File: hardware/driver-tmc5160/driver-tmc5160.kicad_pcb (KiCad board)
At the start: 2 copper layers, 30 x 30 mm, 34 parts, among them J1 Micro-Fit, U1 TMC5160A-TA

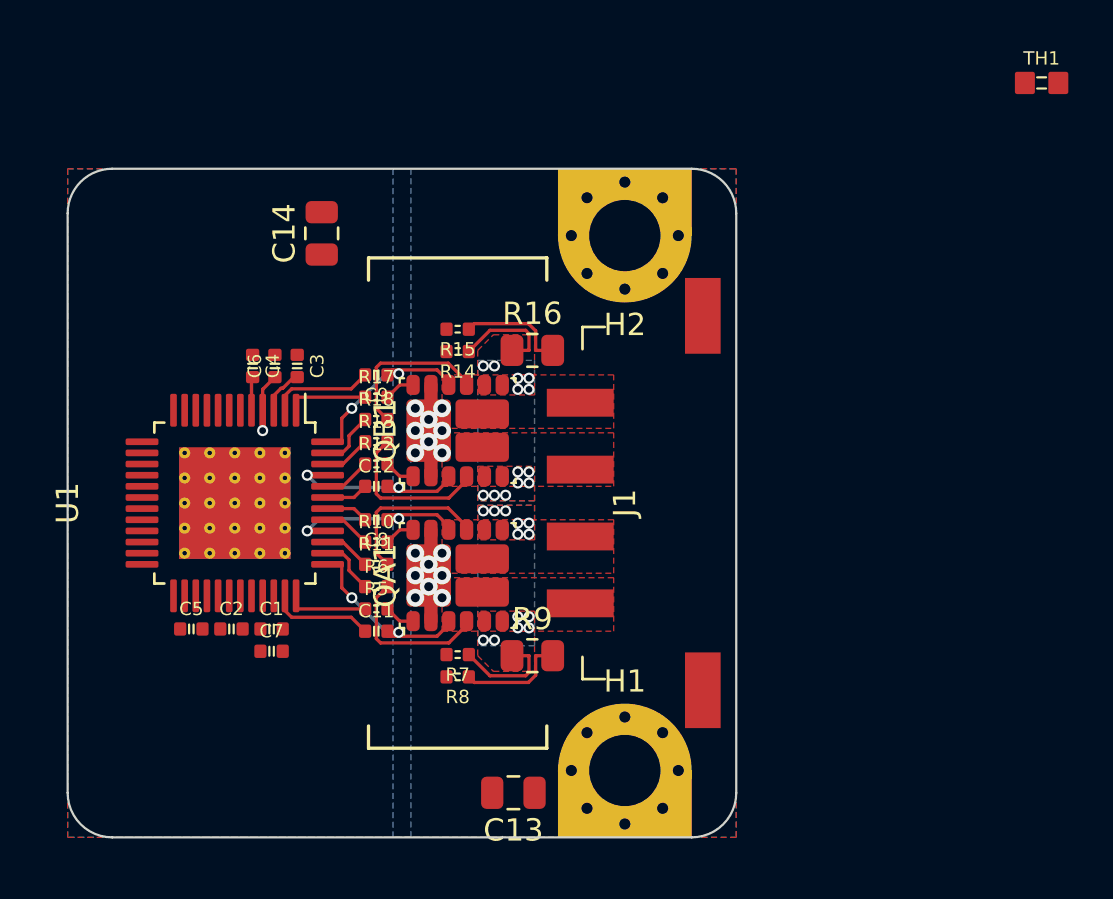
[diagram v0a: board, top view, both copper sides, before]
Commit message: added preliminary LGA layout for motor expansion module
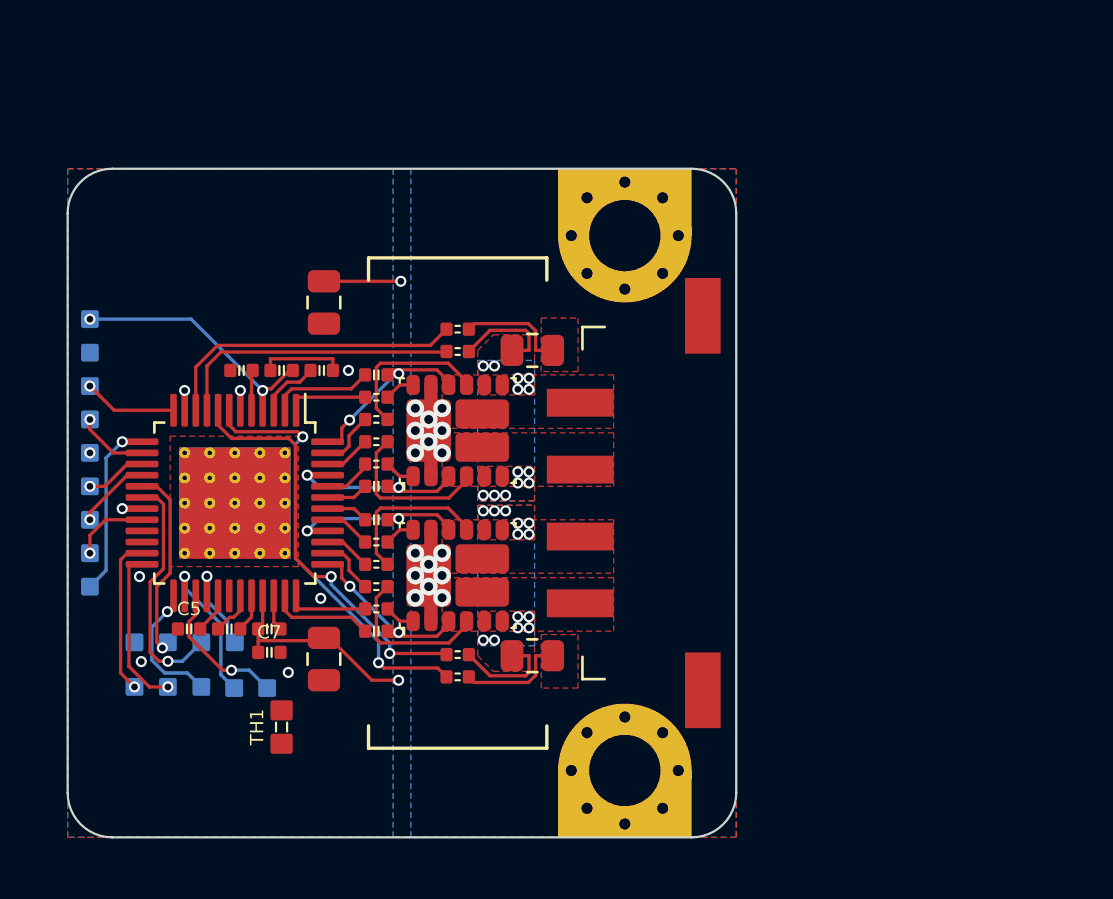
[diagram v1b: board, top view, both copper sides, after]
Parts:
- added T1: 12V, corevus:LGA_Land, B.Cu at (171.0, 46.8)
- added T10: STEP, corevus:LGA_Land, B.Cu at (174.5, 61.2)
- added T11: DIR, corevus:LGA_Land, B.Cu at (176.0, 61.2)
- added T12: EN, corevus:LGA_Land, B.Cu at (177.5, 61.2)
- added T13: CS, corevus:LGA_Land, B.Cu at (171.0, 58.8)
- added T16: DIAG0, corevus:LGA_Land, B.Cu at (177.5, 63.3)
- added T17: DIAG1, corevus:LGA_Land, B.Cu at (178.9, 63.3)
- added T18: ENCA, corevus:LGA_Land, B.Cu at (174.5, 63.2)
- added T19: ENCB, corevus:LGA_Land, B.Cu at (173.0, 63.2)
- added T2: VCCIO, corevus:LGA_Land, B.Cu at (171.0, 57.2)
- added T20: ENCN, corevus:LGA_Land, B.Cu at (176.0, 63.2)
- added T3: GND, corevus:LGA_Land, B.Cu at (171.0, 52.8)
- added T4: CLK, corevus:LGA_Land, B.Cu at (171.0, 49.8)
- added T5: SCK, corevus:LGA_Land, B.Cu at (171.0, 51.2)
- added T6: GND, corevus:LGA_Land, B.Cu at (171.0, 48.2)
- added T7: SDI, corevus:LGA_Land, B.Cu at (171.0, 54.2)
- added T8: SDO, corevus:LGA_Land, B.Cu at (171.0, 55.8)
- added T9: GND, corevus:LGA_Land, B.Cu at (173.0, 61.2)
- H1, H2: footprint tmc5160-driver:edge_mounting_hole -> corevus:MountingHole_M3_Driver
- J1: footprint tmc5160-driver:XKB_X3025WRS-04 -> corevus:XKB_X3025WRS-04
- moved TH1 44.7 mm to (179.6, 65.0), turned to 90 degrees
- moved C13 10.4 mm to (181.5, 62.0), turned to -90 degrees
- moved C14 3.10 mm to (181.5, 46.0), turned to -90 degrees
- moved C3 1.12 mm to (181.4, 49.0), turned to 180 degrees
- moved C4 0.54 mm to (177.8, 49.0), turned to 0 degrees
- moved C6 0.36 mm to (179.6, 49.0), turned to 180 degrees
- moved C7 0.11 mm to (179.1, 61.7)
- moved C5 0.10 mm to (175.4, 60.6)
- moved C1 0.10 mm to (179.1, 60.6)
- moved C2 0.10 mm to (177.2, 60.6)
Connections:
- U1 pad 20: unconnected-(U1-VCC_IO-Pad20) -> VCC
- U1 pad 21: unconnected-(U1-SD_MODE-Pad21) -> VCC
- U1 pad 22: unconnected-(U1-SPI_MODE-Pad22) -> VCC
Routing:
- net /SRAL: track 0.00 -> 19.3 mm, vias 0 -> 2
- net /SRAH: track 0.00 -> 18.6 mm, vias 0 -> 2
- net /SRBL: track 0.00 -> 13.9 mm
- net +48V: track 8.37 -> 21.5 mm, vias 16 -> 18
- net /SRBH: track 0.00 -> 13.0 mm
- net /Dir: track 0.00 -> 10.8 mm, vias 0 -> 1
- net +12V: track 2.63 -> 11.7 mm, vias 1 -> 2
- net /Step: track 0.00 -> 8.51 mm, vias 0 -> 1
- net /~{CS}: track 0.00 -> 7.99 mm, vias 0 -> 1
- net /ENCA: track 0.00 -> 7.80 mm, vias 0 -> 1
- net /ENCB: track 0.00 -> 7.71 mm, vias 0 -> 1
- net /Diag0: track 0.00 -> 6.80 mm, vias 0 -> 1
- net /Diag1: track 0.00 -> 6.41 mm, vias 0 -> 1
- net /ENCN: track 0.00 -> 6.05 mm, vias 0 -> 1
- net /~{En}: track 0.00 -> 4.63 mm, vias 0 -> 1
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
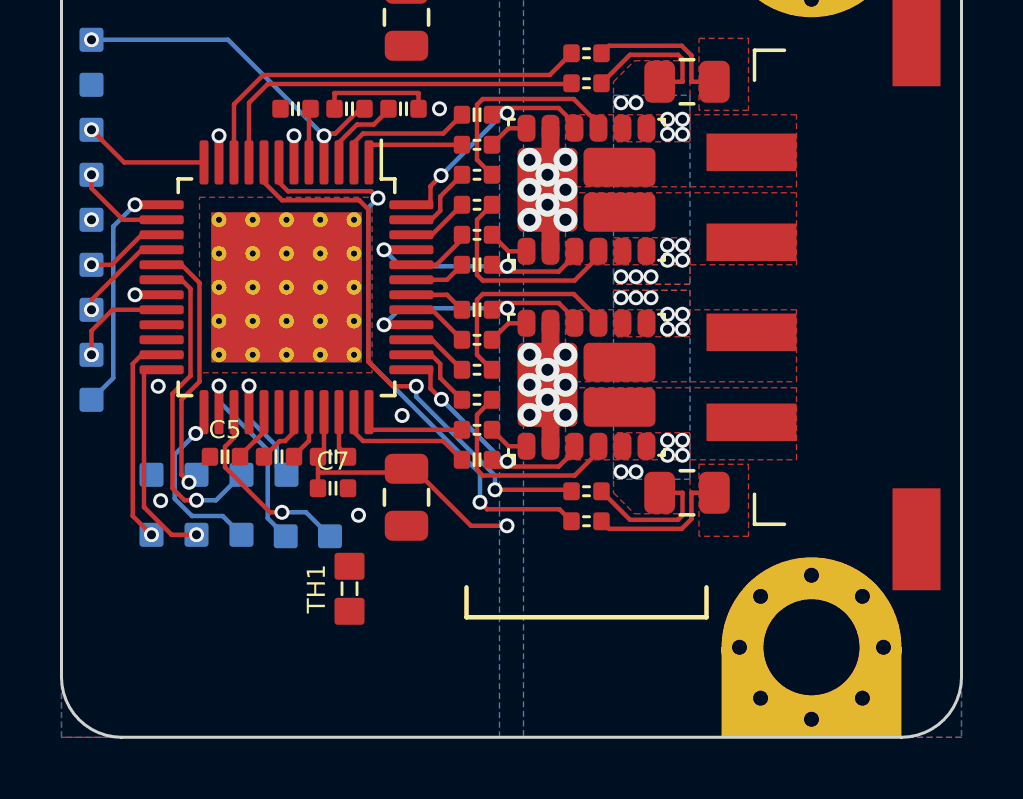
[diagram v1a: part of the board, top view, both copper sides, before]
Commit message: further work on motor drivers and connector layout, additional symbols/footprints/models
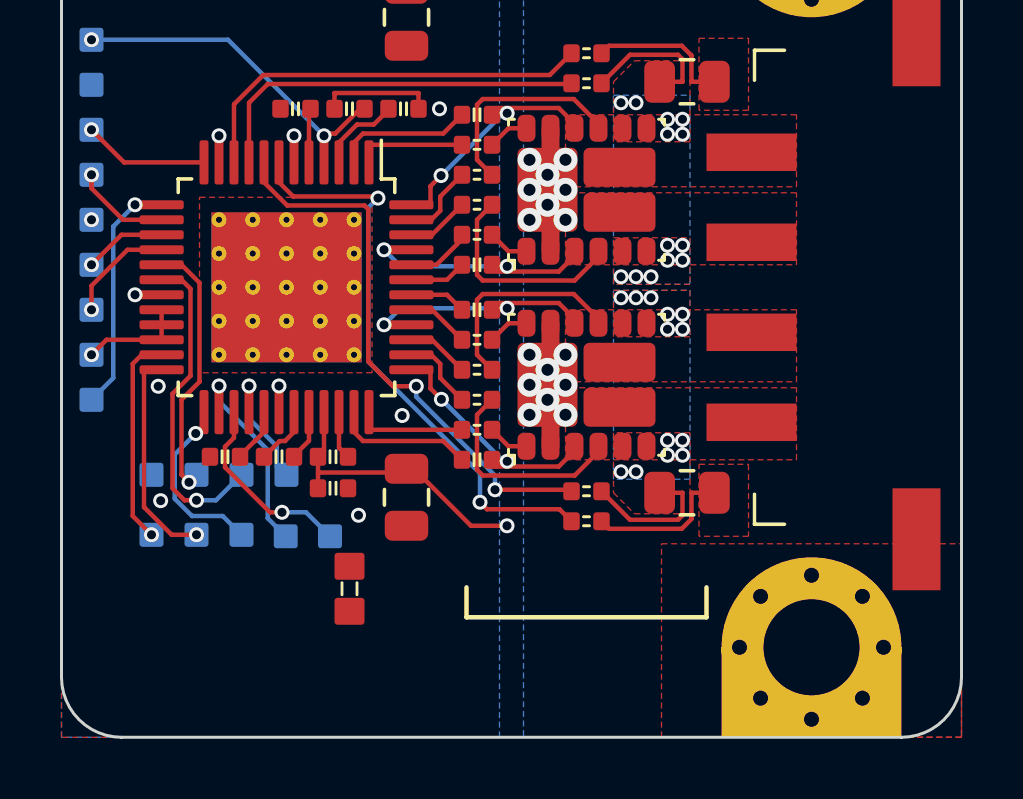
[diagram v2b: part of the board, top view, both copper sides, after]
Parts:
- moved H1 24.0 mm to (195.0, 43.0), turned to 0 degrees
- moved H2 24.0 mm to (195.0, 67.0), turned to 180 degrees
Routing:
- net GND: vias 9 -> 10

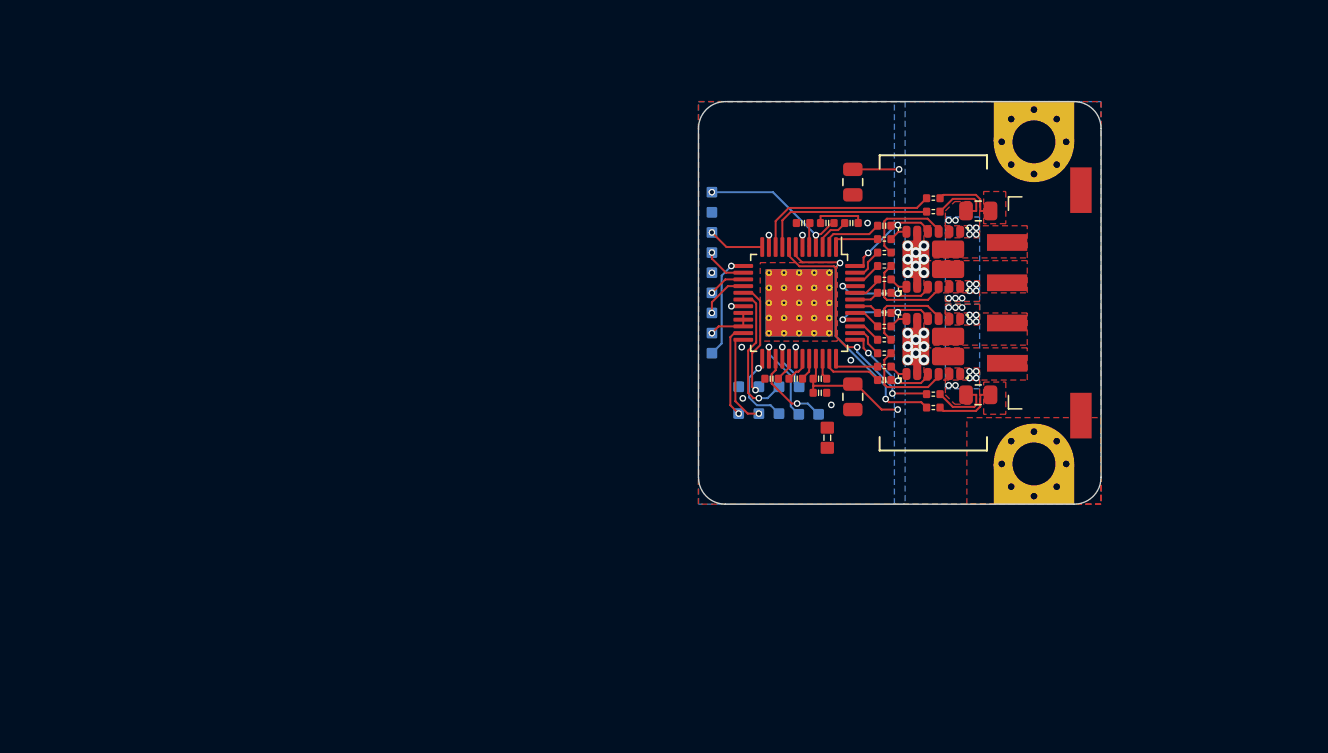
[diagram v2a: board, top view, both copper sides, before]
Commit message: redid mainboard, added probe wiring, replacing ncp chip with LM5160 for now
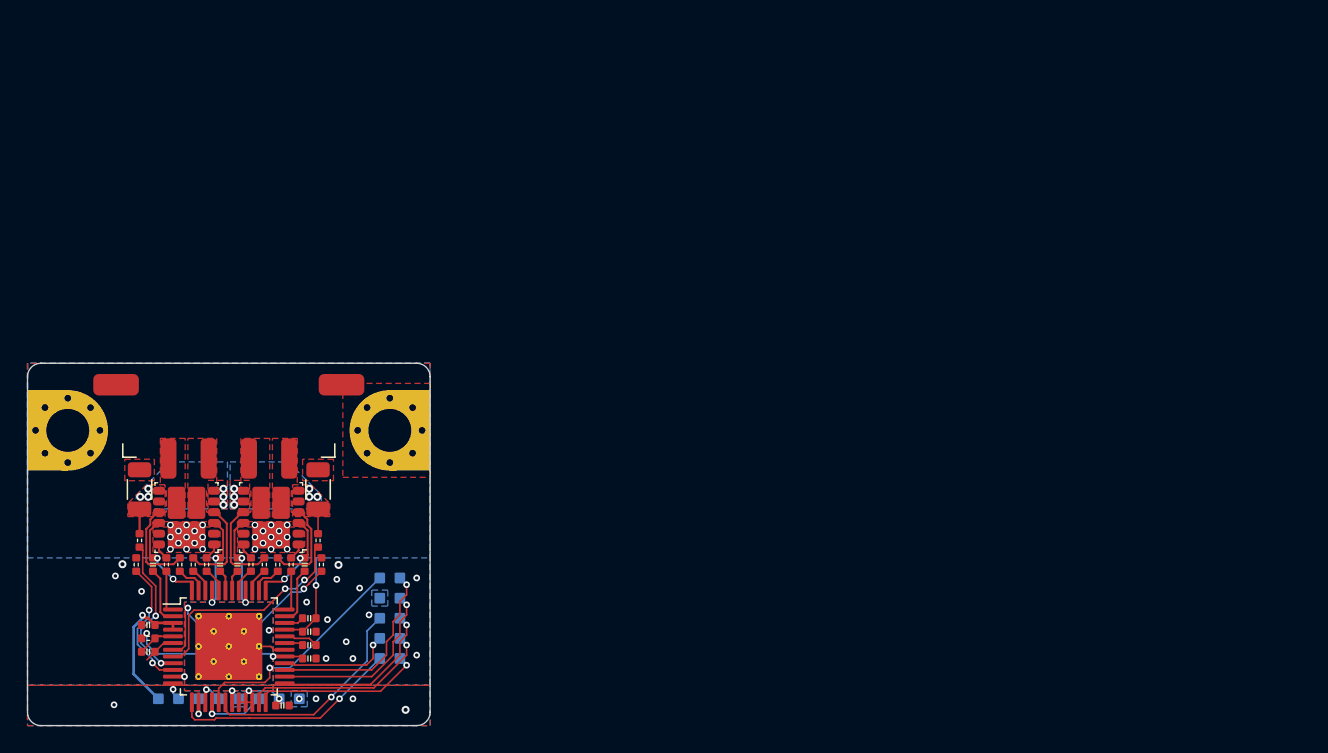
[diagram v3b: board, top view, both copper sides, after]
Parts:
- removed C12: C, AlphaLib:0402C
- removed C13, C14: 1μF, Capacitor_SMD:C_0805_2012Metric
- removed J1: Micro-Fit, corevus:XKB_X3025WRS-04
- removed R16: 30mΩ, Resistor_SMD:R_0805_2012Metric
- removed R17, R18: 10Ω, AlphaLib:0402R
- removed TH1: Thermistor, AlphaLib:0603R
- added C10: 270nF, AlphaLib:0402C, F.Cu at (129.3, 74.5)
- added M1: Micro-Fit 3.0, corevus:XKB_X3025WRS-04D, F.Cu at (135.0, 61.1)
- added R1: 2.2Ω, AlphaLib:0402R, F.Cu at (129.0, 80.0)
- added R2: 10Ω, AlphaLib:0402R, F.Cu at (139.7, 74.5)
- added R3: 10Ω, AlphaLib:0402R, F.Cu at (136.7, 74.5)
- added R4: 10Ω, AlphaLib:0402R, F.Cu at (133.3, 74.5)
- C1: value 100nF 16V -> 2.2μF
- C11, C8, C9: value C -> 270nF
- C2: value 22nF 100V -> 2.2μF
- C3: value 2.2μF -> 470nF
- C4: value 2.2μF -> 100nF
- C6: value 100nF -> 100nF 16V
- C7: value 100nF -> 22nF 100V
- H1: value M3 — VS -> VM
- H2: value M3 — GND -> Gnd
- R10, R11: value 10Ω -> 47Ω
- R12, R13: value 10Ω -> 30mΩ; footprint AlphaLib:0402R -> Resistor_SMD:R_1206_3216Metric
- R7, R8: value 47Ω -> 10Ω
- R9: value 30mΩ -> 10Ω; footprint Resistor_SMD:R_0805_2012Metric -> AlphaLib:0402R
- T1: value 12V -> GND
- T11: value DIR -> GND
- T12: value EN -> DIR
- T13: value CS -> EN
- T2: value VCCIO -> CLK
- T3: value GND -> 12V
- T4: value CLK -> SCK
- T5: value SCK -> GND
- T6: value GND -> SDI
- T7: value SDI -> SDO
- T8: value SDO -> VCC
- T9: value GND -> CS0
- moved H1 75.1 mm to (123.0, 64.5), turned to 90 degrees
- moved R15 65.4 mm to (128.1, 74.5), turned to -90 degrees
- moved R9 60.8 mm to (131.3, 74.5), turned to 90 degrees
- moved QB1 58.9 mm to (131.8, 71.0), turned to 180 degrees
- moved R13 57.9 mm to (128.3, 68.9), turned to 90 degrees
- moved R11 57.5 mm to (128.3, 72.7), turned to -90 degrees
- moved R8 56.4 mm to (132.3, 74.5), turned to 90 degrees
- moved R5 55.5 mm to (130.3, 74.5), turned to 90 degrees
- moved C1 54.0 mm to (129.0, 81.0), turned to 180 degrees
- moved R14 52.6 mm to (141.9, 74.5), turned to -90 degrees
- moved T3 52.1 mm to (129.8, 84.5), turned to 180 degrees
- moved C3 51.8 mm to (141.0, 81.5)
- moved C8 51.7 mm to (135.7, 74.5), turned to 90 degrees
- moved T4 51.7 mm to (132.8, 84.5), turned to 180 degrees
- moved C2 51.6 mm to (129.0, 79.0), turned to 180 degrees
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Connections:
- C1 pad 1: +48V -> GND
- C1 pad 2: Net-(U1-VCP) -> Net-(U1-5VOUT)
- C11 pad 1: /CA2 -> /Motor_B2
- C11 pad 2: /Motor_A2 -> /CB2
- C2 pad 1: Net-(U1-CPO) -> +12V
- C2 pad 2: Net-(U1-CPI) -> GND
- C3 pad 2: Net-(U1-12VOUT) -> Net-(U1-VCC)
- C4 pad 1: GND -> +48V
- C4 pad 2: Net-(U1-5VOUT) -> GND
- C5 pad 2: Net-(U1-VCC) -> VCC
- C6 pad 1: +12V -> Net-(U1-VCP)
- C6 pad 2: GND -> +48V
- C7 pad 1: +48V -> Net-(U1-CPI)
- C7 pad 2: GND -> Net-(U1-CPO)
- C8 pad 1: /Motor_A1 -> /CA1
- C8 pad 2: /CA1 -> /Motor_A1
- C9 pad 1: /Motor_B1 -> /Motor_A2
- C9 pad 2: /CB1 -> /CA2
- R10 pad 1: /HA1 -> Net-(QA1-S2-Pad5)
- R10 pad 2: Net-(QA1-G4) -> /SRAH
- R11 pad 1: /LA1 -> Net-(QB1-S2-Pad5)
- R11 pad 2: Net-(QA1-G3) -> /SRBH
- R12 pad 1: /HB2 -> Net-(QA1-S2-Pad5)
- R12 pad 2: Net-(QB1-G1) -> GND
- R13 pad 1: /LB2 -> Net-(QB1-S2-Pad5)
- R13 pad 2: Net-(QB1-G2) -> GND
- R14 pad 1: Net-(QB1-S2-Pad5) -> GND
- R14 pad 2: /SRBH -> /SRAL
- R5 pad 1: /HA2 -> /HB1
- R5 pad 2: Net-(QA1-G1) -> Net-(QB1-G4)
- R7 pad 1: Net-(QA1-S2-Pad5) -> /LA1
- R7 pad 2: /SRAH -> Net-(QA1-G3)
- R8 pad 1: GND -> /LB2
- R8 pad 2: /SRAL -> Net-(QB1-G2)
- R9 pad 1: Net-(QA1-S2-Pad5) -> /LB1
- R9 pad 2: GND -> Net-(QB1-G3)
- T1 pad 1: +12V -> GND
- T11 pad 1: /Dir -> GND
- T12 pad 1: /~{En} -> /Dir
- T13 pad 1: /~{CS} -> /~{En}
- T2 pad 1: VCC -> /Clk
- T3 pad 1: GND -> +12V
- T4 pad 1: /Clk -> /SCK
- T5 pad 1: /SCK -> GND
- T6 pad 1: GND -> /SDI
- T7 pad 1: /SDI -> /SDO
- T8 pad 1: /SDO -> VCC
- T9 pad 1: GND -> /~{CS}
- U1 pad 3: Net-(U1-12VOUT) -> +12V
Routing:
- net +48V: track 21.5 -> 7.31 mm, vias 18 -> 27
- net Net-(U1-VCC): track 1.78 -> 13.4 mm, vias 0 -> 2
- net /~{CS}: track 7.99 -> 17.2 mm
- net GND: track 14.3 -> 5.19 mm, vias 10 -> 22
- net /Step: track 8.51 -> 17.5 mm
- net /Diag1: track 6.41 -> 14.6 mm
- net /Diag0: track 6.80 -> 13.6 mm
- net /ENCN: track 6.05 -> 12.7 mm
- net /ENCB: track 7.71 -> 14.3 mm
- net /Dir: track 10.8 -> 16.5 mm
- net /ENCA: track 7.80 -> 12.7 mm
- net /SRBL: track 13.9 -> 9.95 mm, vias 0 -> 2
- net /~{En}: track 4.63 -> 8.55 mm
- net /SRAL: track 19.3 -> 16.1 mm
- net Net-(QA1-S2-Pad5): track 4.67 -> 1.84 mm, vias 13 -> 6
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- added copper zone on F.Cu, net +48V
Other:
- board size 30 x 30 mm -> 30 x 27 mm

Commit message: nearing first prototype woot! copyediting over entire board, fixed some mistakes
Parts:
- added C12: 100nF 60V/2, AlphaLib:0402C, F.Cu at (142.4, 79.0)
- added C13: 47nF 100V, AlphaLib:0402C, F.Cu at (141.0, 80.5)
- C4: value 100nF -> 100nF 60V/2
- C7: value 22nF 100V -> 47nF 100V/2
- moved C7 1.49 mm to (142.4, 81.0), turned to -90 degrees
- moved T10 1.00 mm to (146.2, 74.5)
- moved T11 1.00 mm to (146.2, 76.0)
- moved T12 1.00 mm to (146.2, 77.5)
- moved T13 1.00 mm to (146.2, 79.0)
- moved T16 1.00 mm to (147.8, 76.0)
- moved T17 1.00 mm to (147.8, 74.5)
- moved T18 1.00 mm to (147.8, 80.5)
- moved T19 1.00 mm to (147.8, 79.0)
- moved T20 1.00 mm to (147.8, 77.5)
- moved T9 1.00 mm to (146.2, 80.5)
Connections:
- C4 pad 2: GND -> Net-(C12-Pad1)
- C7 pad 2: Net-(U1-CPO) -> Net-(C13-Pad1)
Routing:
- net GND: track 5.19 -> 7.57 mm, vias 22 -> 21
- net Net-(C13-Pad1): track 0.00 -> 1.33 mm
- net /~{CS}: track 17.2 -> 18.2 mm
- net /Dir: track 16.5 -> 17.5 mm
- net Net-(C12-Pad1): track 0.00 -> 0.94 mm
- net Net-(U1-CPI): track 2.61 -> 3.51 mm
- net /~{En}: track 8.55 -> 9.27 mm
- net /Diag1: track 14.6 -> 15.2 mm

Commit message: test new gitignore with completed mainboard
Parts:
- added REF**: ToolingHole, corevus:ToolingHole, F.Cu at (148.5, 69.0)
- added REF**: ToolingHole, corevus:ToolingHole, F.Cu at (121.5, 85.0)
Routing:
- net GND: vias 21 -> 15
